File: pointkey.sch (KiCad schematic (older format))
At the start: 12 parts, among them P1 CONN_01X02, SW1 SW_PUSH, SW2 SW_PUSH, U1 4013

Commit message: debounce
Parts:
- removed C2: C, Capacitors_ThroughHole:C_Radial_D5_L6_P2.5, symbol C
- removed D2, D3: LED, LEDs:LED-3MM, symbol LED
- removed R4: R, Discret:R3-5, symbol R
- removed SW2: SW_PUSH, Buttons_Switches_ThroughHole:SW_PUSH_SMALL, symbol SW_PUSH
- added C?: C, symbol C
- added D? (x2): D, symbol D
- added K?: RELAY_2RT, symbol RELAY_2RT
- added Q?: BC546, TO-92, symbol BC546
- added R?: 10k, symbol R
- C1: value C -> 1u; footprint Capacitors_ThroughHole:C_Radial_D5_L6_P2.5 -> (none)
- R1: renamed from R3; value R -> 510k
- R2: renamed from R1; value R -> 22k
- R2: value R -> 22k; footprint Discret:R3-5 -> (none)
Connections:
- net GND: now also U1.3 (Cp), U1.5 (D), Q?.3 (E); no longer U1.10 (Cd), U1.4 (Cd), U1.6 (Sd)
- net VCC: now also C?.1, D?.1 (K), K?.8
- net at R2.1, SW1.1: now also U1.6 (Sd); no longer C1.1, U1.3 (Cp)
- net at R1.2, U1.1 (Q): now also U1.11 (Cp), D?.1 (K)
- net at U1.2 (~Q): no longer U1.5 (D)
- net at R1.1: now also C1.1, U1.4 (Cd), D?.2 (A)
- net at R2.1: now also U1.10 (Cd), C?.2; no longer U1.11 (Cp)
- net at U1.13 (Q): now also R?.2
- new net: Q?.2 (B), R?.1
- new net: D?.2 (A), K?.9, Q?.1 (C)
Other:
- moved on the sheet: R1, R2, SW1, U1A, U1B

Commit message: components
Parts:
- removed K?: RELAY_2RT, symbol RELAY_2RT
- removed Q?: BC546, TO-92, symbol BC546
- added K1: RELAY_1RT, symbol RELAY_1RT
- added P2: CONN_01X03, symbol CONN_01X03
- added Q?: КТ315, кт-13, symbol КТ315
- gave numbers to parts that had none: 4
- renumbered R2 to R1, R1 to R2, R2 to R3
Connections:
- net GND: now also Q?.3 (E)
- net VCC: now also K1.2
- net at R4.1: now also Q?.2 (B)
- net at D2.2 (A): now also K1.1, Q?.1 (C)
- new net: K1.3, P2.1 (P1)
- new net: K1.4, P2.3 (P3)
- new net: K1.5, P2.2 (P2)
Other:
- moved on the sheet: C2, D2, R3, R4

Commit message: new pcb
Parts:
- C1: footprint (none) -> Capacitors_ThroughHole:C_Radial_D5_L6_P2.5
- C2: value C -> 20u; footprint (none) -> Capacitors_ThroughHole:C_Radial_D5_L6_P2.5
- D1, D2: footprint (none) -> Discret:D4
- K1: footprint (none) -> kicad_my_library:RELAY_812H_1C_C
- P2: footprint (none) -> Pin_Headers:Pin_Header_Straight_1x03
- Q1: renamed from Q?; footprint кт-13 -> kicad_my_library:кт-13
- R3, R4: footprint (none) -> Discret:R3-5
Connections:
- no-connect marks 0 -> 1
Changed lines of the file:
@@
 F 0 "C1" H 5175 3300 50  0000 L CNN
 F 1 "1u" H 5175 3100 50  0000 L CNN
-F 2 "" H 5188 3050 50  0000 C CNN
+F 2 "Capacitors_ThroughHole:C_Radial_D5_L6_P2.5" H 5188 3050 50  0001 C CNN
 F 3 "" H 5150 3200 50  0000 C CNN
 	1    5150 3200
@@
 F 0 "D1" H 5500 2550 50  0000 C CNN
 F 1 "D" H 5500 2350 50  0000 C CNN
-F 2 "" H 5500 2450 50  0000 C CNN
+F 2 "Discret:D4" H 5500 2450 50  0001 C CNN
 F 3 "" H 5500 2450 50  0000 C CNN
 	1    5500 2450
@@
 F 0 "R3" V 6030 3200 50  0000 C CNN
 F 1 "22k" V 5950 3200 50  0000 C CNN
-F 2 "" V 5880 3200 50  0000 C CNN
+F 2 "Discret:R3-5" V 5880 3200 50  0001 C CNN
 F 3 "" H 5950 3200 50  0000 C CNN
 	1    5950 3200
@@
 P 5950 2600
 F 0 "C2" H 5975 2700 50  0000 L CNN
-F 1 "C" H 5975 2500 50  0000 L CNN
-F 2 "" H 5988 2450 50  0000 C CNN
+F 1 "20u" H 5975 2500 50  0000 L CNN
+F 2 "Capacitors_ThroughHole:C_Radial_D5_L6_P2.5" H 5988 2450 50  0001 C CNN
 F 3 "" H 5950 2600 50  0000 C CNN
 	1    5950 2600
@@
 F 0 "R4" V 7980 2000 50  0000 C CNN
 F 1 "10k" V 7900 2000 50  0000 C CNN
-F 2 "" V 7830 2000 50  0000 C CNN
+F 2 "Discret:R3-5" V 7830 2000 50  0001 C CNN
 F 3 "" H 7900 2000 50  0000 C CNN
 	1    7900 2000
@@
 F 0 "K1" H 9300 1300 50  0000 C CNN
 F 1 "RELAY_1RT" H 9500 600 50  0000 C CNN
-F 2 "" H 9350 1100 50  0000 C CNN
+F 2 "kicad_my_library:RELAY_812H_1C_C" H 9350 1100 50  0001 C CNN
 F 3 "" H 9350 1100 50  0000 C CNN
 	1    9350 1100
 	1    0    0    -1
 $EndComp
-Connection ~ 2700 3500
-Wire Wire Line
-	2700 3000 2700 3500
-Connection ~ 2700 2200
-Wire Wire Line
-	2700 2100 2700 2700
-Connection ~ 2700 1350
-Wire Wire Line
-	2700 1350 2700 1500
-Connection ~ 1950 2200
-Wire Wire Line
-	1750 2200 1950 2200
-Connection ~ 1750 2000
-Wire Wire Line
-	1750 2000 1750 2200
-Connection ~ 2300 1350
-Wire Wire Line
-	1400 1450 1950 1450
-Wire Wire Line
-	3900 3500 3900 2450
-Connection ~ 3900 3500
-Wire Wire Line
-	1950 1450 1950 3500
-Connection ~ 2300 1000
-Wire Wire Line
-	1350 2600 1350 2450
-Wire Wire Line
-	1350 2450 1950 2450
-Connection ~ 1950 2450
-Wire Wire Line
-	1950 1150 1950 1350
-Connection ~ 1950 1350
-Wire Wire Line
-	3000 1500 3000 2200
-Wire Wire Line
-	3000 2200 2700 2200
-Wire Wire Line
-	4100 2750 4100 2900
-Wire Wire Line
-	3500 2000 3300 2000
-Wire Wire Line
-	3300 2000 3300 3500
-Connection ~ 3300 3500
-Wire Wire Line
-	3500 2200 3300 2200
-Connection ~ 3300 2200
-Wire Wire Line
-	4100 1500 3000 1500
-Wire Wire Line
-	4700 2000 5500 2000
-Wire Wire Line
-	5500 2000 5850 2200
-Wire Wire Line
-	5500 2000 5500 2300
-Wire Wire Line
-	5150 2300 5150 2000
-Connection ~ 5150 2000
-Wire Wire Line
-	5150 2600 5150 3050
-Wire Wire Line
-	4100 2900 5500 2900
-Connection ~ 5150 2900
-Wire Wire Line
-	5500 2900 5500 2600
-Wire Wire Line
-	5150 3500 5150 3350
-Wire Wire Line
-	1950 3500 8600 3500
-Wire Wire Line
-	3900 1350 3900 1950
-Wire Wire Line
-	4100 1650 4100 1500
-Wire Wire Line
-	5850 2200 6150 2200
-Connection ~ 5500 2000
-Wire Wire Line
-	6050 1550 7450 1550
-Wire Wire Line
-	7450 1550 7450 2900
-Wire Wire Line
-	7450 2400 7350 2400
-Wire Wire Line
-	6750 1650 6750 1450
-Wire Wire Line
-	6750 1450 7550 1450
-Wire Wire Line
-	7550 1450 7550 3500
-Connection ~ 5150 3500
-Wire Wire Line
-	6750 2900 6750 2750
-Wire Wire Line
-	5950 2900 6750 2900
-Wire Wire Line
-	6150 2000 6050 2000
-Wire Wire Line
-	6050 2000 6050 1550
-Wire Wire Line
-	5950 2750 5950 3050
-Wire Wire Line
-	5950 3350 5950 3500
-Connection ~ 5950 3500
-Connection ~ 5950 2900
-Connection ~ 3900 1350
-Wire Wire Line
-	5950 1350 5950 2450
-Wire Wire Line
-	7350 2000 7750 2000
-Wire Wire Line
-	8050 2000 8300 2000
-Connection ~ 7550 3500
-Connection ~ 5950 1350
-Wire Wire Line
-	2300 1350 2300 1000
-Wire Wire Line
-	1400 1350 8950 1350
-Wire Wire Line
-	8950 1450 8950 2000
 $Comp
 L CONN_01X03 P2
@@
 F 0 "P2" H 10300 1150 50  0000 C CNN
 F 1 "CONN_01X03" V 10400 950 50  0000 C CNN
-F 2 "" H 10300 950 50  0000 C CNN
+F 2 "Pin_Headers:Pin_Header_Straight_1x03" H 10300 950 50  0001 C CNN
 F 3 "" H 10300 950 50  0000 C CNN
 	1    10300 950
 	1    0    0    -1
 $EndComp
-Wire Wire Line
-	9750 1250 9950 1250
-Wire Wire Line
-	9950 1250 9950 1050
-Wire Wire Line
-	9950 1050 10100 1050
-Wire Wire Line
-	9750 1050 9750 950
-Wire Wire Line
-	9750 950  10100 950
-Wire Wire Line
-	8950 1150 8950 850
-Wire Wire Line
-	8950 850  10100 850
 $Comp
 L PWR_FLAG #FLG05
@@
 	1    0    0    -1
 $EndComp
-Wire Wire Line
-	7150 2750 7150 2900
-Wire Wire Line
-	7150 2900 7450 2900
-Connection ~ 7450 2400
-$Comp
-L КТ315 Q?
+$Comp
+L КТ315 Q1
 U 1 1 56917754
 P 8500 2500
-F 0 "Q?" H 8700 2575 50  0000 L CNN
+F 0 "Q1" H 8700 2575 50  0000 L CNN
 F 1 "КТ315" H 8700 2500 50  0000 L CNN
-F 2 "кт-13" H 8700 2425 50  0000 L CIN
+F 2 "kicad_my_library:кт-13" H 8700 2425 50  0000 L CIN
 F 3 "" H 8500 2500 50  0000 L CNN
 	1    8500 2500
 	1    0    0    -1
 $EndComp
-Wire Wire Line
-	8600 3500 8600 2700
-Wire Wire Line
-	8300 2000 8300 2500
-Wire Wire Line
-	8600 1800 8600 2300
-Wire Wire Line
-	8850 2150 8850 2150
-Wire Wire Line
-	8950 2000 8600 2000
 $Comp
 L D D2
@@
 F 0 "D2" H 8600 1750 50  0000 C CNN
 F 1 "D" H 8600 1550 50  0000 C CNN
-F 2 "" H 8600 1650 50  0000 C CNN
+F 2 "Discret:D4" H 8600 1650 50  0001 C CNN
 F 3 "" H 8600 1650 50  0000 C CNN
 	1    8600 1650
 	0    1    1    0
 $EndComp
+NoConn ~ 4700 2400
+Connection ~ 2700 3500
+Wire Wire Line
+	2700 3000 2700 3500
+Connection ~ 2700 2200
+Wire Wire Line
+	2700 2100 2700 2700
+Connection ~ 2700 1350
+Wire Wire Line
+	2700 1350 2700 1500
+Connection ~ 1950 2200
+Wire Wire Line
+	1750 2200 1950 2200
+Connection ~ 1750 2000
+Wire Wire Line
+	1750 2000 1750 2200
+Connection ~ 2300 1350
+Wire Wire Line
+	1400 1450 1950 1450
+Wire Wire Line
+	3900 3500 3900 2450
+Connection ~ 3900 3500
+Wire Wire Line
+	1950 1450 1950 3500
+Connection ~ 2300 1000
+Wire Wire Line
+	1350 2600 1350 2450
+Wire Wire Line
+	1350 2450 1950 2450
+Connection ~ 1950 2450
+Wire Wire Line
+	1950 1150 1950 1350
+Connection ~ 1950 1350
+Wire Wire Line
+	3000 1500 3000 2200
+Wire Wire Line
+	3000 2200 2700 2200
+Wire Wire Line
+	4100 2750 4100 2900
+Wire Wire Line
+	3500 2000 3300 2000
+Wire Wire Line
+	3300 2000 3300 3500
+Connection ~ 3300 3500
+Wire Wire Line
+	3500 2200 3300 2200
+Connection ~ 3300 2200
+Wire Wire Line
+	4100 1500 3000 1500
+Wire Wire Line
+	4700 2000 5500 2000
+Wire Wire Line
+	5500 2000 5850 2200
+Wire Wire Line
+	5500 2000 5500 2300
+Wire Wire Line
+	5150 2300 5150 2000
+Connection ~ 5150 2000
+Wire Wire Line
+	5150 2600 5150 3050
+Wire Wire Line
+	4100 2900 5500 2900
+Connection ~ 5150 2900
+Wire Wire Line
+	5500 2900 5500 2600
+Wire Wire Line
+	5150 3500 5150 3350
+Wire Wire Line
+	1950 3500 8600 3500
+Wire Wire Line
+	3900 1350 3900 1950
+Wire Wire Line
+	4100 1650 4100 1500
+Wire Wire Line
+	5850 2200 6150 2200
+Connection ~ 5500 2000
+Wire Wire Line
+	6050 1550 7450 1550
+Wire Wire Line
+	7450 1550 7450 2900
+Wire Wire Line
+	7450 2400 7350 2400
+Wire Wire Line
+	6750 1650 6750 1450
+Wire Wire Line
+	6750 1450 7550 1450
+Wire Wire Line
+	7550 1450 7550 3500
+Connection ~ 5150 3500
+Wire Wire Line
+	6750 2900 6750 2750
+Wire Wire Line
+	5950 2900 6750 2900
+Wire Wire Line
+	6150 2000 6050 2000
+Wire Wire Line
+	6050 2000 6050 1550
+Wire Wire Line
+	5950 2750 5950 3050
+Wire Wire Line
+	5950 3350 5950 3500
+Connection ~ 5950 3500
+Connection ~ 5950 2900
+Connection ~ 3900 1350
+Wire Wire Line
+	5950 1350 5950 2450
+Wire Wire Line
+	7350 2000 7750 2000
+Wire Wire Line
+	8050 2000 8300 2000
+Connection ~ 7550 3500
+Connection ~ 5950 1350
+Wire Wire Line
+	2300 1350 2300 1000
+Wire Wire Line
+	1400 1350 8950 1350
+Wire Wire Line
+	8950 1450 8950 2000
+Wire Wire Line
+	9750 1250 9950 1250
+Wire Wire Line
+	9950 1250 9950 1050
+Wire Wire Line
+	9950 1050 10100 1050
+Wire Wire Line
+	9750 1050 9750 950
+Wire Wire Line
+	8950 1150 8950 850
+Wire Wire Line
+	7150 2750 7150 2900
+Wire Wire Line
+	7150 2900 7450 2900
+Connection ~ 7450 2400
+Wire Wire Line
+	8600 3500 8600 2700
+Wire Wire Line
+	8300 2000 8300 2500
+Wire Wire Line
+	8600 1800 8600 2300
+Wire Wire Line
+	8850 2150 8850 2150
+Wire Wire Line
+	8950 2000 8600 2000
 Connection ~ 8600 2000
 Wire Wire Line
 	8600 1500 8600 1350
 Connection ~ 8600 1350
+Wire Wire Line
+	9750 950  10100 950
+Wire Wire Line
+	8950 850  10100 850
 $EndSCHEMATC

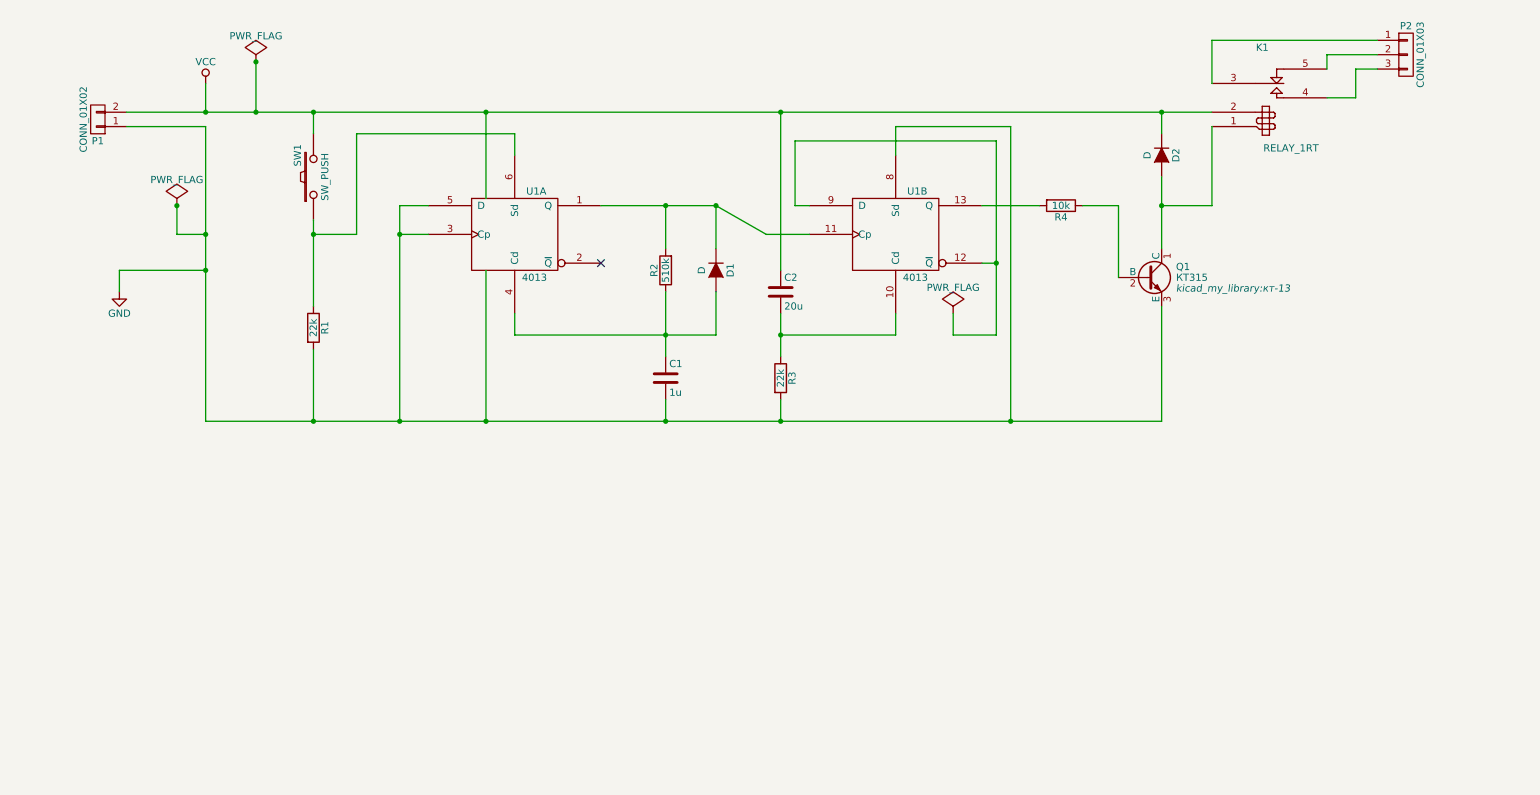
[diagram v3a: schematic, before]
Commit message: transistor key for indicator led
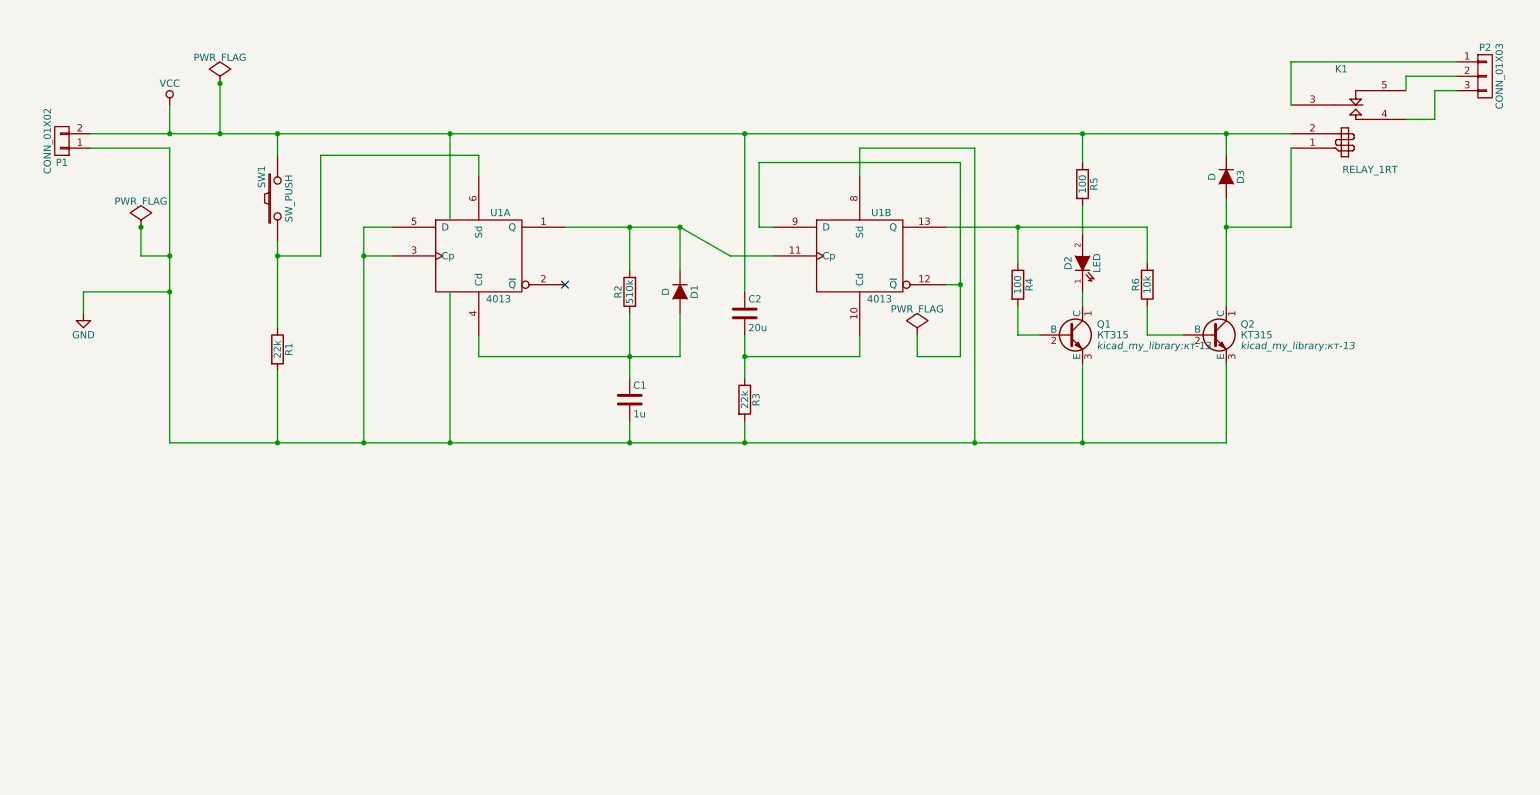
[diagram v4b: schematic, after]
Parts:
- added D2: LED, LEDs:LED-3MM, symbol LED
- added Q1: КТ315, kicad_my_library:кт-13, symbol КТ315
- added R4, R5: 100, Discret:R3-5, symbol R
- renumbered D2 to D3, Q1 to Q2, R4 to R6
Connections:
- net GND: now also Q1.3 (E)
- net VCC: now also R5.1
- net at R6.2, U1.13 (Q): now also R4.1
- new net: Q1.2 (B), R4.2
- new net: D2.1 (K), Q1.1 (C)
- new net: D2.2 (A), R5.2
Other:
- moved on the sheet: C1, C2, D1, D3, K1, P1, P2, Q2, R1, R2, R3, R6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

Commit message: dispatcher
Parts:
- removed P2: CONN_01X03, Pin_Headers:Pin_Header_Straight_1x03, symbol CONN_01X03
- added P2, P3: CONN_01X02, Connect:AK300-2, symbol CONN_01X02
- added Q2, Q3: КТ315, kicad_my_library:кт-13, symbol КТ315
- added R6: 100, Discret:R3-5, symbol R
- added R7: 1K, Discret:R3-5, symbol R
- P1: footprint Pin_Headers:Pin_Header_Straight_1x02 -> Connect:AK300-2
- R8: renamed from R6; value 10k -> 1k
- renumbered Q2 to Q4
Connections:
- net GND: now also Q2.3 (E)
- net VCC: now also K1.1, R5.2, Q3.1 (C), R7.1; no longer K1.2, R5.1
- net SWI_1: now reaches R1.1, SW1.1, U1.6 (Sd)
- net SWI_1: now also P3.2 (P2)
- net at R4.1, R8.2, U1.13 (Q): now also R6.2
- net at D3.2 (A), Q4.1 (C): now also K1.2; no longer K1.1
- net at K1.3: now also P2.1 (P1)
- net at K1.5: now also P2.2 (P2)
- net at D2.2 (A): now also R5.1; no longer R5.2
- new net: Q2.2 (B), R6.1
- new net: Q2.1 (C), Q3.2 (B), R7.2
- new net IND_1: P3.1 (P1), Q3.3 (E)
- no-connect marks 1 -> 2
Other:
- moved on the sheet: C1, C2, D1, D2, D3, K1, Q1, Q4, R1, R2, R3, R4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
